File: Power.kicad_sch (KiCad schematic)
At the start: 28 parts, among them U3 LMR51420YDDCR, U4 LM317MDCYR

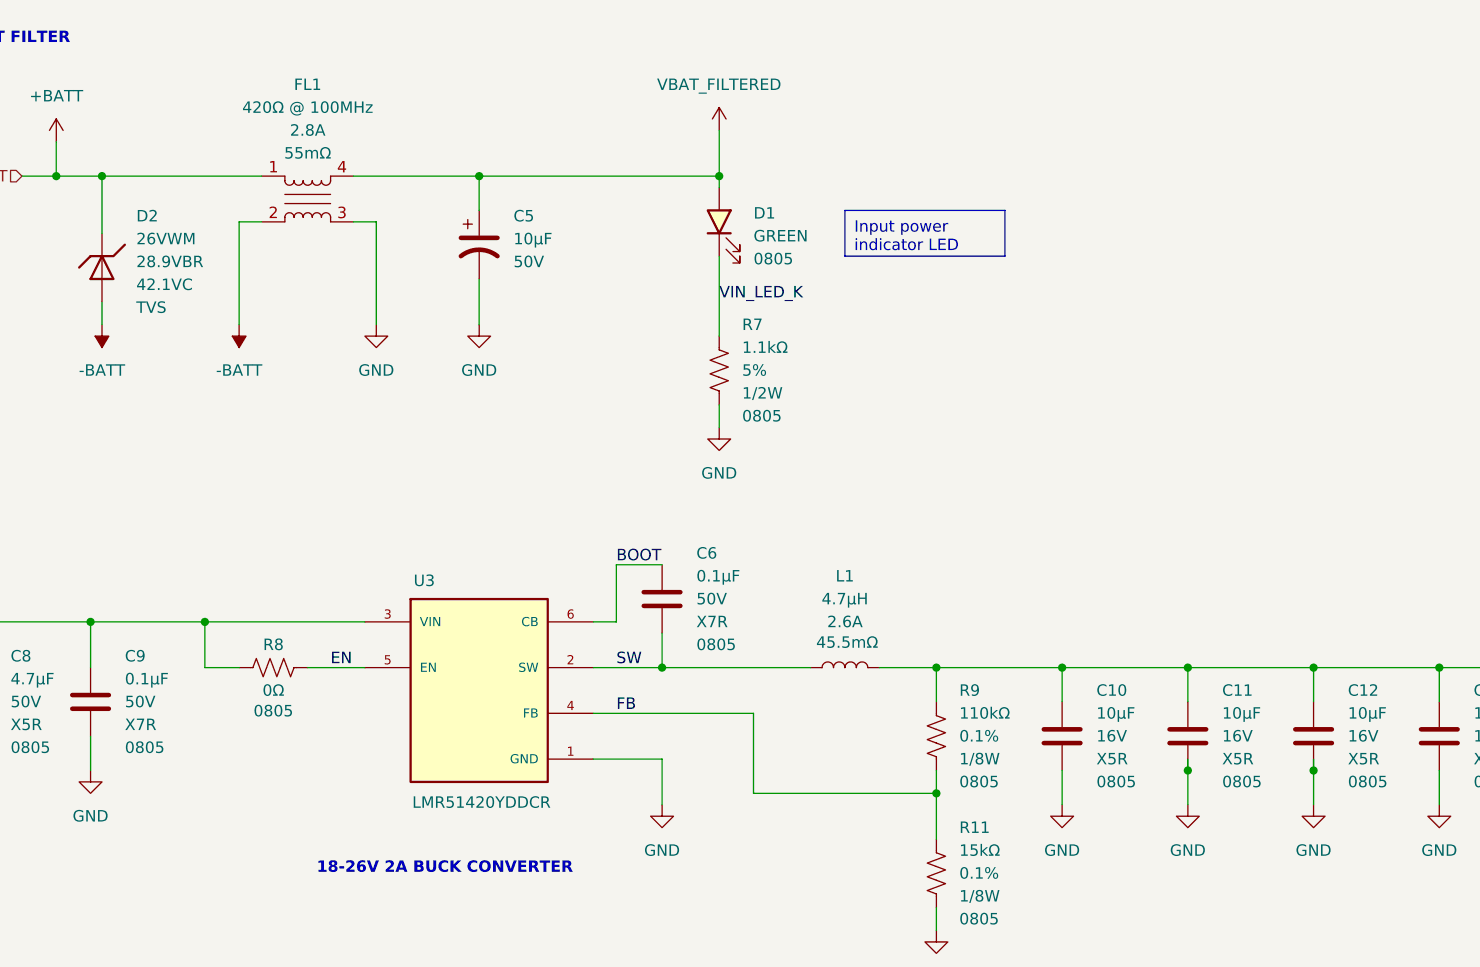
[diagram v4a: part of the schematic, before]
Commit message: pcb routing completed
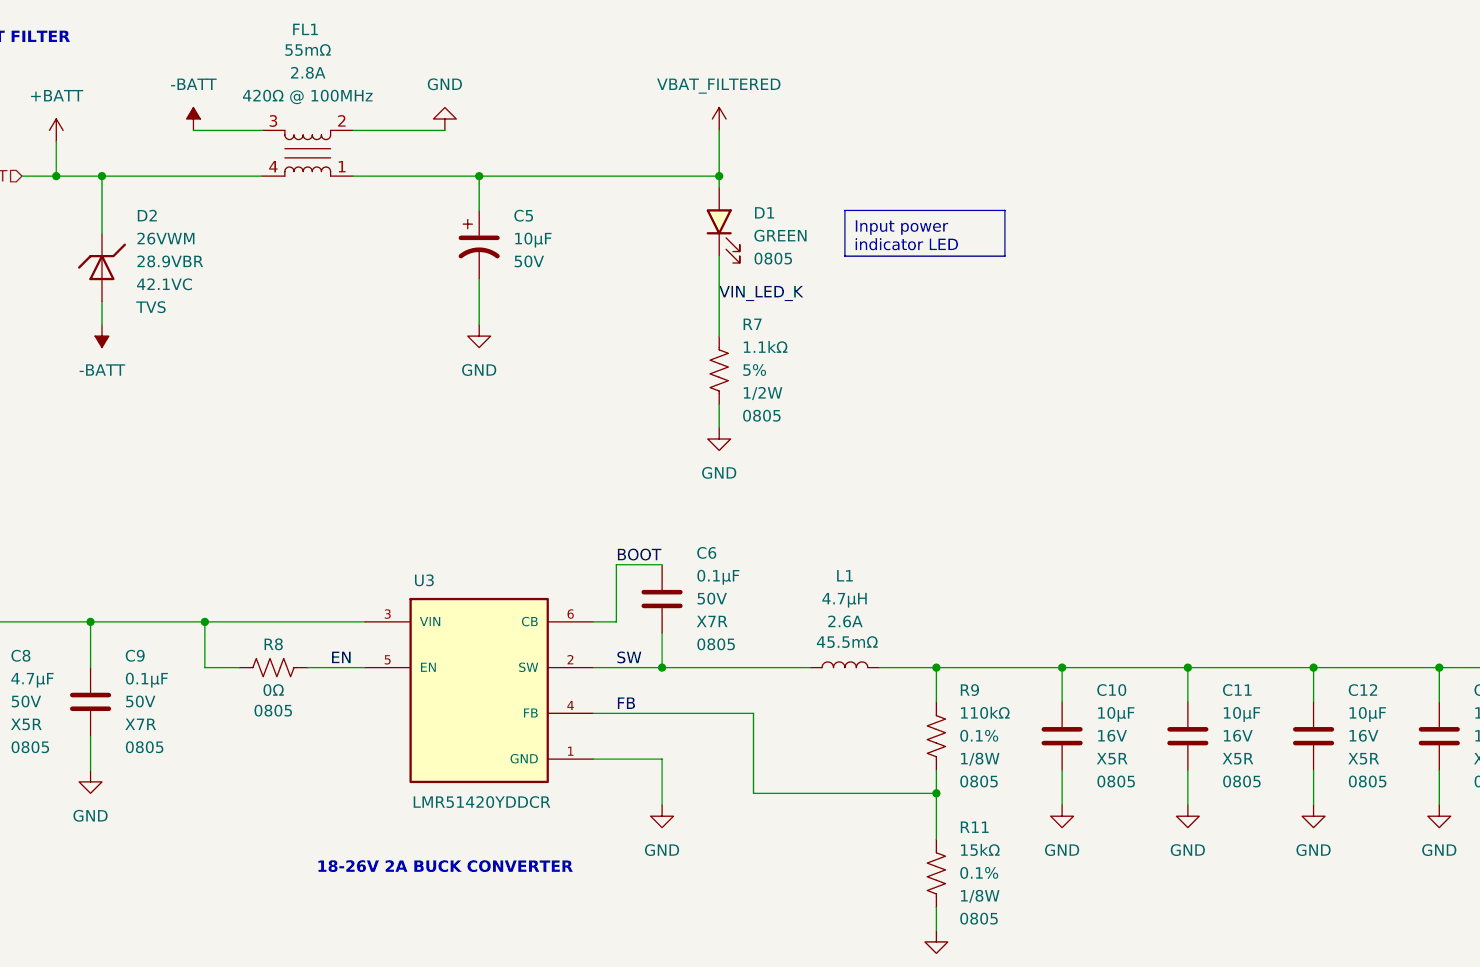
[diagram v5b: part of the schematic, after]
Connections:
- net +BATT: now also FL1.4; no longer FL1.1
- net -BATT: now also FL1.3; no longer FL1.2
- net GND: now also FL1.2; no longer FL1.3
- net VBAT_FILTERED: now also FL1.1; no longer FL1.4

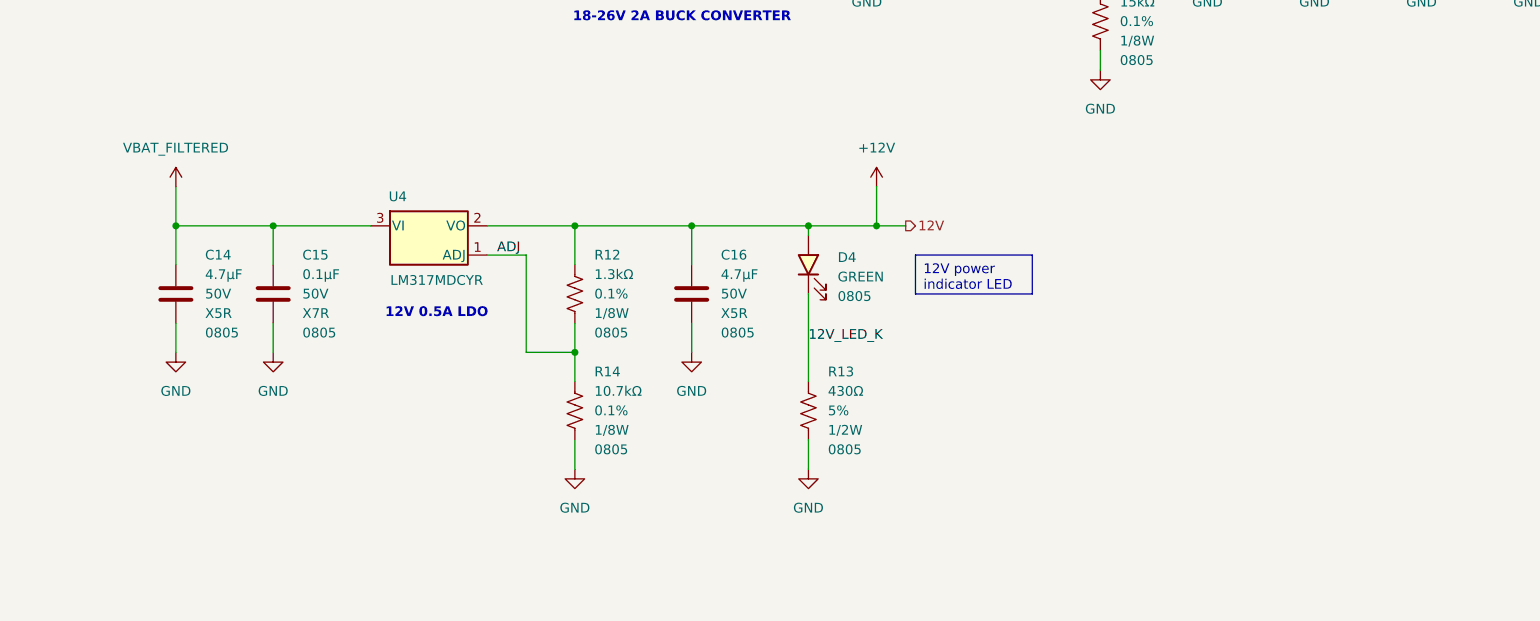
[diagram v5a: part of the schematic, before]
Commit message: added i2c + another servo rail
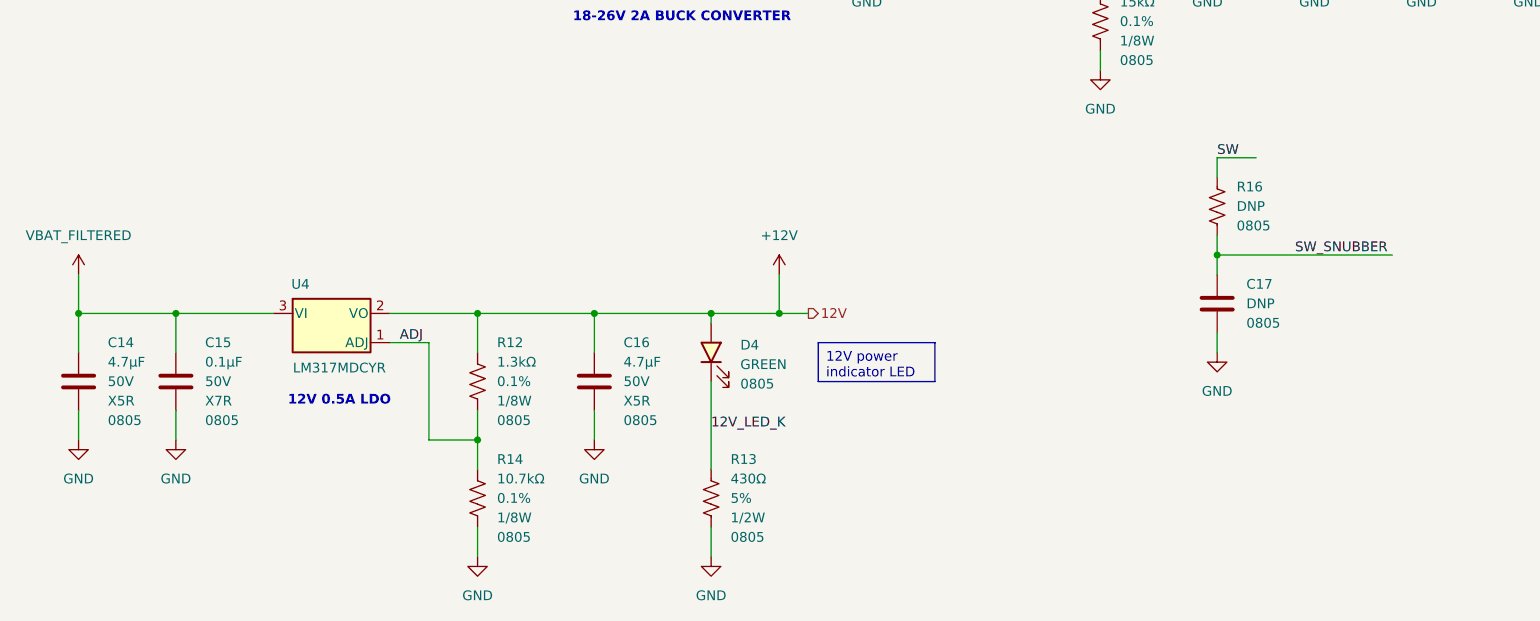
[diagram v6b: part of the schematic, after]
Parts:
- added C17: DNP, Capacitor_SMD:C_0805_2012Metric_Pad1.18x1.45mm_HandSolder, symbol Capacitors_MLCC:DNP_MLCC_0805
- added R16: DNP 0805, Resistor_SMD:R_0805_2012Metric_Pad1.20x1.40mm_HandSolder, symbol Resistors:DNP_0805
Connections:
- net GND: now also C17.2
- net SW: now also R16.1
- new net SW_SNUBBER: C17.1, R16.2
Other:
- moved on the sheet: C14, C15, C16, D4, R12, R13, R14, U4

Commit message: 2nd rev is done
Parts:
- removed D1: 150080GS75000, LED_SMD:LED_0805_2012Metric_Pad1.15x1.40mm_HandSolder, symbol LED:150080GS75000
- removed R7: ERJ-P06J112V, Resistor_SMD:R_0805_2012Metric_Pad1.20x1.40mm_HandSolder, symbol Resistors:ERJ-P06J112V
- added D3: 150080GS75000, LED_SMD:LED_0805_2012Metric_Pad1.15x1.40mm_HandSolder, symbol LED:150080GS75000
- added Q1: DMN3731U-7, Package_TO_SOT_SMD:SOT-23-3_DMN3731U-7, symbol Transistor_FET:DMN3731U-7
- added R12: ERJ-P06J112V, Resistor_SMD:R_0805_2012Metric_Pad1.20x1.40mm_HandSolder, symbol Resistors:ERJ-P06J112V
- renumbered C9 to C10, C10 to C11, C11 to C12, C12 to C13, C13 to C14, C17 to C15, C14 to C16, C15 to C17, C16 to C18, C5 to C6, C6 to C7, C7 to C8, C8 to C9, D3 to D4, D4 to D5, R8 to R13, R9 to R14, R11 to R15, R10 to R16, R16 to R17, R12 to R18, R14 to R19, R13 to R20
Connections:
- net +BATT: now also D3.2 (A)
- net GND: now also Q1.2 (S)
- net VIN_LED_K: now also D3.1 (K), R12.1
- new net VIN_LED: Q1.1 (G)
- new net VIN_LED_FET_D: Q1.3 (D), R12.2
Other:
- moved on the sheet: C10, C11, C12, C13, C14, C15, C16, C17, C18, C7, C8, C9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

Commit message: ordered PCB
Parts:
- C15, R17: now not fitted
- R20: value ERJ-P06J112V -> ERJ-P06J431V
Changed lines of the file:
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@@
 		(in_bom yes)
 		(on_board yes)
-		(dnp no)
+		(dnp yes)
 		(fields_autoplaced yes)
 		(property "Reference" "R17"
@@
 		(in_bom yes)
 		(on_board yes)
-		(dnp no)
+		(dnp yes)
 		(fields_autoplaced yes)
 		(property "Reference" "C15"
@@
 			)
 		)
-		(property "Value" "ERJ-P06J112V"
+		(property "Value" "ERJ-P06J431V"
 			(at 123.698 204.978 0)
 			(effects
